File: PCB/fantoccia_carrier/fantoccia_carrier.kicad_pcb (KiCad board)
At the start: 2 copper layers, 108 x 131.5 mm, 13 parts, among them J1 BU2450SM-JJ-GTR, J2 1881545, J3 1881545, J4 1881545, J5 1881545, U1 NUCLEO144-H743ZI, U2 TXS0108EPWR, U3 TXS0108EPWR

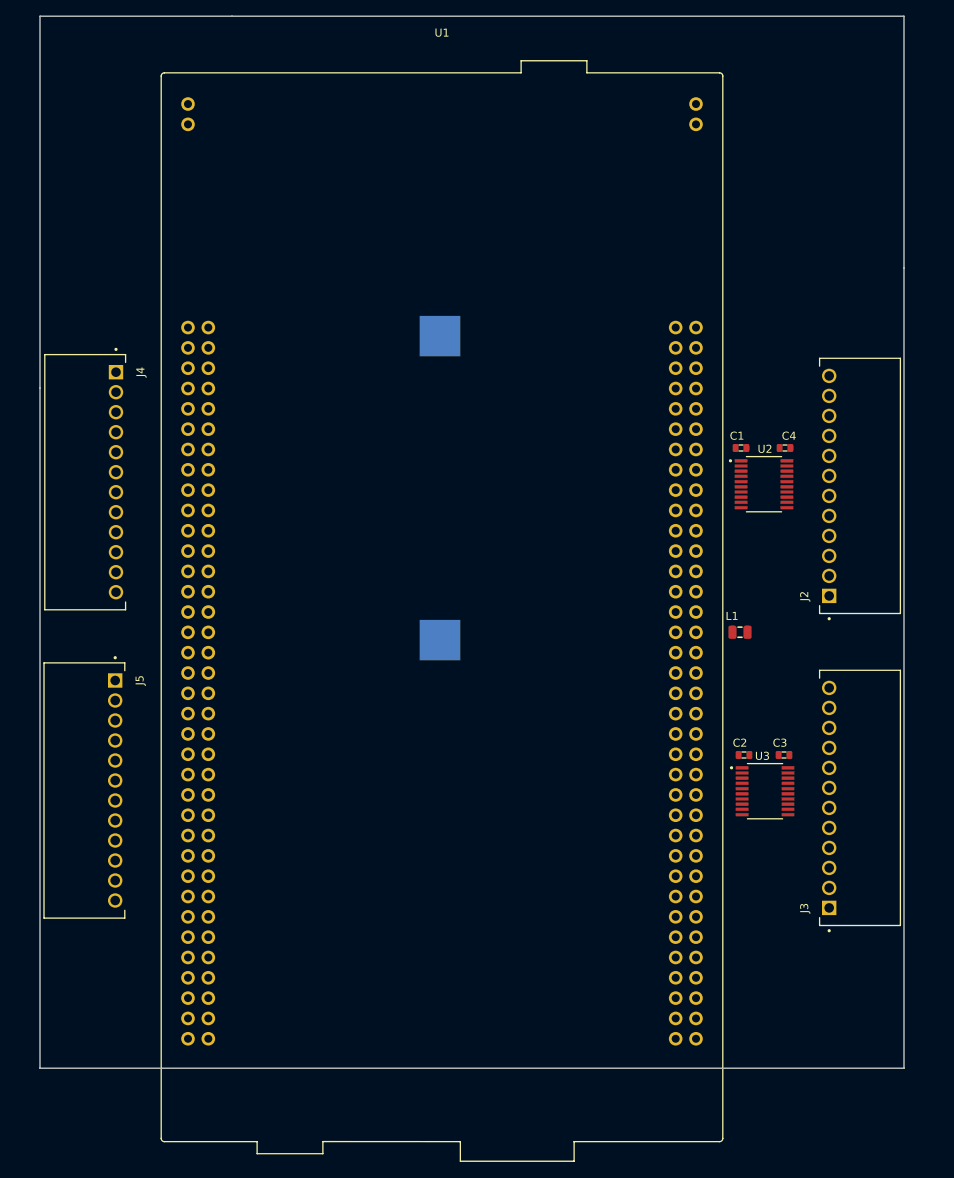
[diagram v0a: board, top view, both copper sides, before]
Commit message: PCB progress and feature updates
Added another bank of 5V channels. PCB layout figured out, board shape defined. 3D model added to STM32 evaluation kit. Now just need to determine pinout and add protection circuitry to pins.
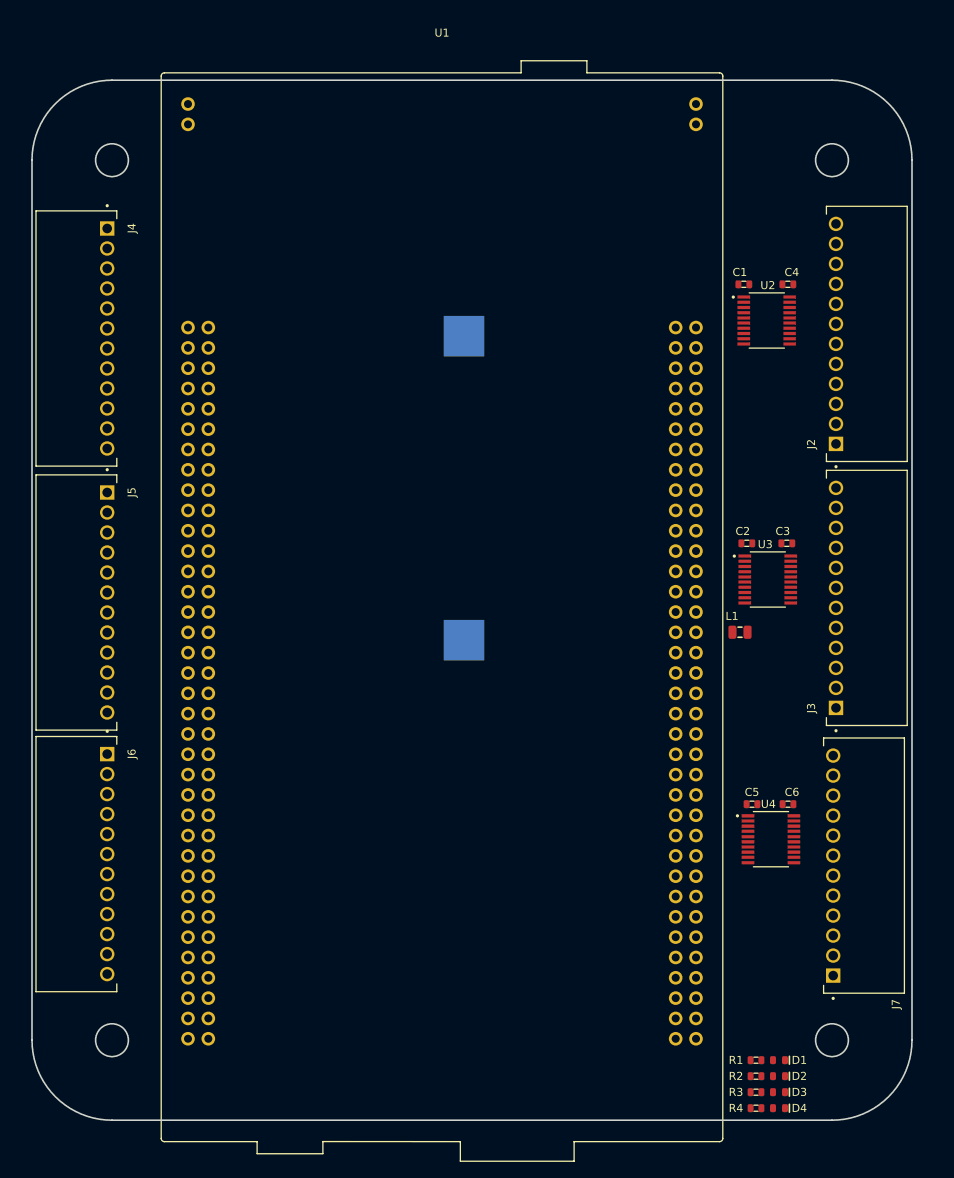
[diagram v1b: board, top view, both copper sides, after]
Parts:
- added C5: CGA3E2X7R1H104K080AA, AVR-KiCAD-Lib-Capacitors:C0603, F.Cu at (194.0, 117.0)
- added C6: CGA3E2X7R1H104K080AA, AVR-KiCAD-Lib-Capacitors:C0603, F.Cu at (198.5, 117.0)
- added D1: LTST-C194TBKT, AVR-KiCAD-Lib-Diodes:LED0603, F.Cu at (197.4, 149.0)
- added D2: LTST-C194TBKT, AVR-KiCAD-Lib-Diodes:LED0603, F.Cu at (197.4, 151.0)
- added D3: LTST-C194TBKT, AVR-KiCAD-Lib-Diodes:LED0603, F.Cu at (197.4, 153.0)
- added D4: LTST-C194TBKT, AVR-KiCAD-Lib-Diodes:LED0603, F.Cu at (197.4, 155.0)
- added J6: 1881545, AVR-KiCAD-Lib-Connectors:PHOENIX_1881545, F.Cu at (104.5, 108.5)
- added J7: 1881545, AVR-KiCAD-Lib-Connectors:PHOENIX_1881545, F.Cu at (213.1, 140.6)
- added R1: RC0603FR-072K2L, AVR-KiCAD-Lib-Resistors:R0603, F.Cu at (194.5, 149.0)
- added R2: RC0603FR-072K2L, AVR-KiCAD-Lib-Resistors:R0603, F.Cu at (194.5, 151.0)
- added R3: RC0603FR-072K2L, AVR-KiCAD-Lib-Resistors:R0603, F.Cu at (194.5, 153.0)
- added R4: RC0603FR-072K2L, AVR-KiCAD-Lib-Resistors:R0603, F.Cu at (194.5, 155.0)
- added U4: TXS0108EPWR, AVR-KiCAD-Lib-ICs:SOP65P640X120-20N, F.Cu at (196.4, 121.4)
- moved U3 26.5 mm to (196.0, 88.9)
- moved C2 26.5 mm to (193.3, 84.4)
- moved C3 26.5 mm to (198.3, 84.4)
- moved J3 25.0 mm to (213.4, 107.2)
- moved J5 23.5 mm to (104.5, 75.8)
- moved U2 20.5 mm to (195.8, 56.5)
- moved C1 20.5 mm to (193.0, 52.0)
- moved C4 20.5 mm to (198.5, 52.0)
- moved J2 19.0 mm to (213.4, 74.2)
- moved J4 18.0 mm to (104.5, 42.8)
- moved J1 3.00 mm to (158.0, 77.5)
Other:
- board size 108 x 131.5 mm -> 110 x 130 mm

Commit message: Design Rules
Created Design rules, added more IO connections, need to figure out pinning next.
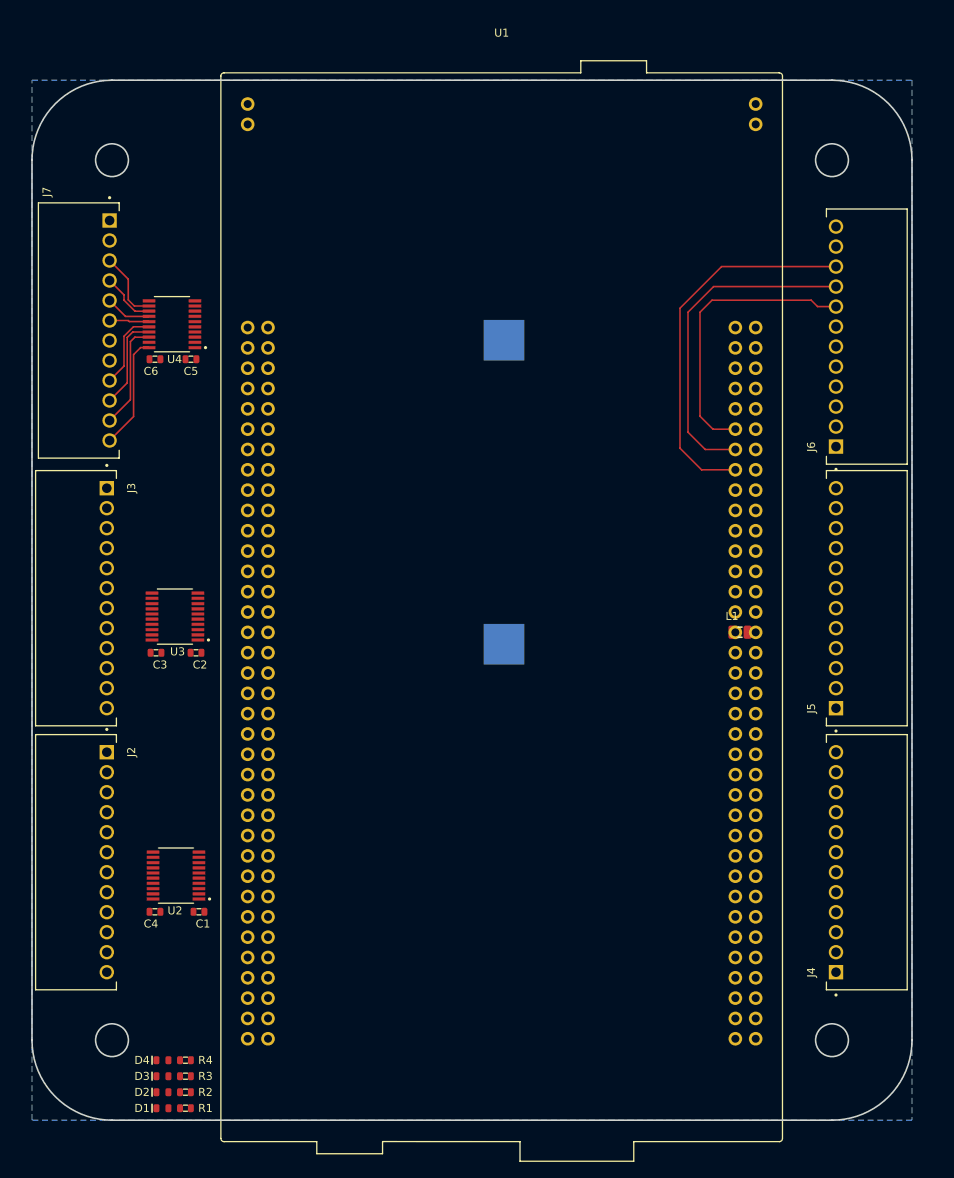
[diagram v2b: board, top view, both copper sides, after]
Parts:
- moved J7 146.6 mm to (104.8, 41.8), turned to -90 degrees
- moved J4 146.1 mm to (213.4, 140.2), turned to 90 degrees
- moved J2 114.2 mm to (104.5, 108.3), turned to -90 degrees
- moved J6 114.1 mm to (213.4, 74.5), turned to 90 degrees
- moved J3 113.5 mm to (104.5, 75.3), turned to -90 degrees
- moved J5 113.3 mm to (213.4, 107.2), turned to 90 degrees
- moved C4 111.4 mm to (119.4, 130.4), turned to 180 degrees
- moved C1 103.9 mm to (124.9, 130.4), turned to 0 degrees
- moved U2 101.3 mm to (122.0, 125.9), turned to 180 degrees
- moved U4 98.7 mm to (121.5, 57.0), turned to 180 degrees
- moved C6 96.7 mm to (119.4, 61.4), turned to 180 degrees
- moved C5 89.5 mm to (123.9, 61.4), turned to 0 degrees
- moved C3 80.0 mm to (119.5, 98.1), turned to 180 degrees
- moved D1 77.3 mm to (120.3, 155.0), turned to 180 degrees
- moved D4 77.3 mm to (120.3, 149.0), turned to 180 degrees
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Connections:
- J6 pad 1: unconnected-(J6-Pin_1-Pad1) -> /Nucleo/3.3V_GPIO16
- J6 pad 10: unconnected-(J6-Pin_10-Pad10) -> /Nucleo/3.3V_GPIO23
- J6 pad 2: unconnected-(J6-Pin_2-Pad2) -> /Nucleo/3.3V_GPIO17
- J6 pad 3: unconnected-(J6-Pin_3-Pad3) -> /Nucleo/3.3V_GPIO18
- J6 pad 4: unconnected-(J6-Pin_4-Pad4) -> /Nucleo/3.3V_GPIO19
- J6 pad 7: unconnected-(J6-Pin_7-Pad7) -> /Nucleo/3.3V_GPIO20
- J6 pad 8: unconnected-(J6-Pin_8-Pad8) -> /Nucleo/3.3V_GPIO21
- J6 pad 9: unconnected-(J6-Pin_9-Pad9) -> /Nucleo/3.3V_GPIO22
- U1 pad 83: unconnected-(U1-PA5-Pad83) -> /Nucleo/3.3V_GPIO21
- U1 pad 85: unconnected-(U1-PA6-Pad85) -> /Nucleo/3.3V_GPIO22
- U1 pad 87: unconnected-(U1-ETH_CRS_DV/PA7-Pad87) -> /Nucleo/3.3V_GPIO23
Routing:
- net /Nucleo/3.3V_GPIO23: track 0.00 -> 47.2 mm
- net /Nucleo/3.3V_GPIO22: track 0.00 -> 41.6 mm
- net /Nucleo/3.3V_GPIO21: track 0.00 -> 36.0 mm
- net /Translator 5V/5V_GPIO16: track 0.00 -> 14.3 mm
- net /Translator 5V/5V_GPIO17: track 0.00 -> 13.5 mm
- net /Translator 5V/5V_GPIO18: track 0.00 -> 11.8 mm
- net /Translator 5V/5V_GPIO19: track 0.00 -> 9.90 mm
- net /Translator 5V/5V_GPIO23: track 0.00 -> 8.81 mm
- net /Translator 5V/5V_GPIO22: track 0.00 -> 6.91 mm
- net /Translator 5V/5V_GPIO21: track 0.00 -> 5.75 mm
- net /Translator 5V/5V_GPIO20: track 0.00 -> 4.99 mm
- added copper zone on B.Cu, net GND

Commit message: PCB and Pinout
Progress made with PCB wiring eval board pins to pheonix connectors. Pinout almost completely chosen but subject to revision !
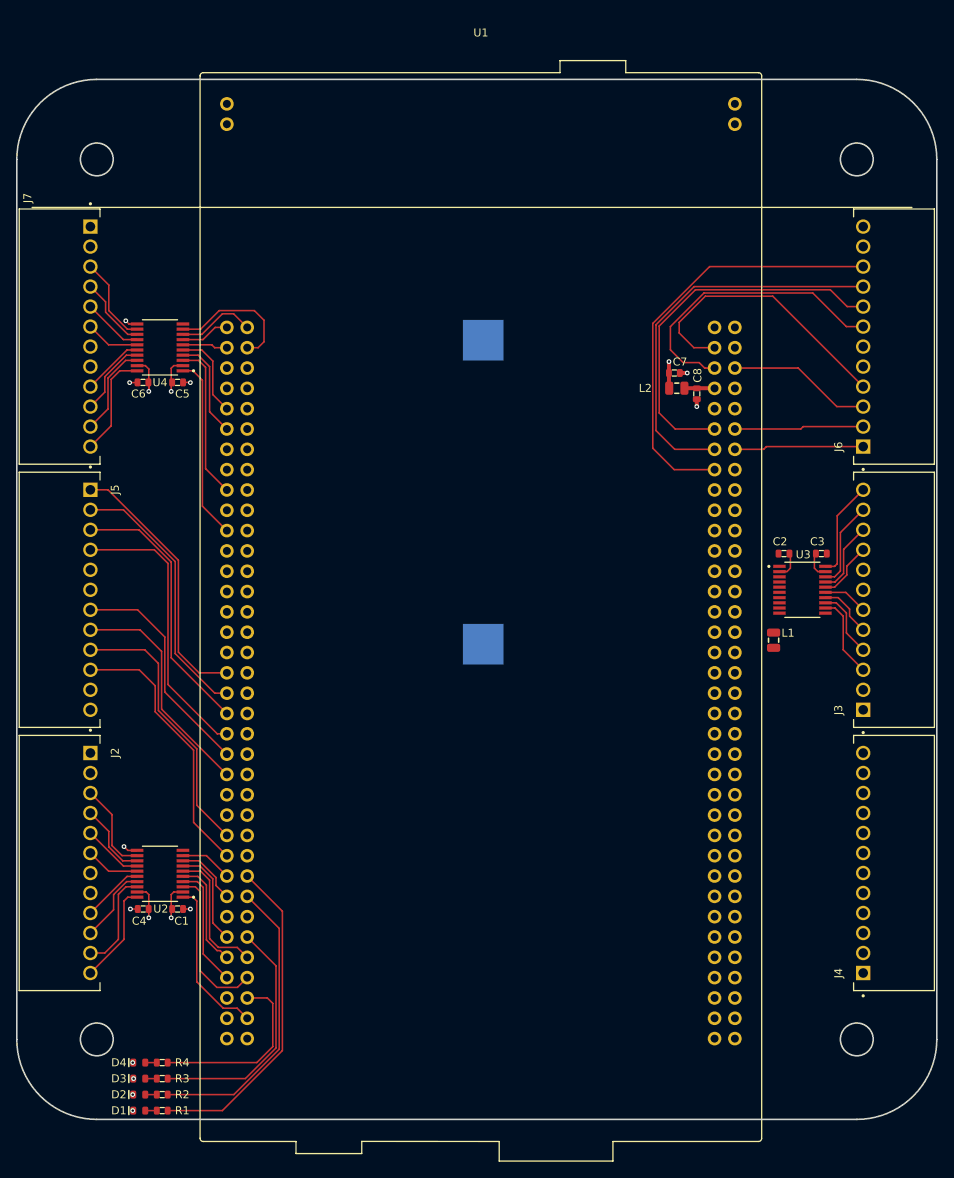
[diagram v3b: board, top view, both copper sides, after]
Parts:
- added C7: CGA3E2X7R1H104K080AA, AVR-KiCAD-Lib-Capacitors:C0603, F.Cu at (184.3, 63.1)
- added C8: CGA3E2X7R1H104K080AA, AVR-KiCAD-Lib-Capacitors:C0603, F.Cu at (187.1, 65.7)
- added L2: HZ0805E601R-10, AVR-KiCAD-Lib-Inductors:HZ0805E601R-10, F.Cu at (184.6, 65.0)
- moved J3 116.8 mm to (216.8, 107.4), turned to 90 degrees
- moved J5 115.4 mm to (102.4, 75.5), turned to -90 degrees
- moved C3 84.1 mm to (202.7, 85.7), turned to 0 degrees
- moved U3 78.5 mm to (200.3, 90.2), turned to 0 degrees
- moved C2 74.5 mm to (198.0, 85.7), turned to 180 degrees
- moved L1 4.32 mm to (196.7, 96.5), turned to -90 degrees
- moved J4 3.40 mm to (216.8, 140.3)
- moved J6 3.40 mm to (216.8, 74.5)
- moved C5 3.35 mm to (122.2, 64.3)
- moved C6 3.26 mm to (117.9, 64.3)
- moved U4 3.26 mm to (120.0, 59.9)
- moved D1 2.92 mm to (117.4, 155.3)
- moved D2 2.92 mm to (117.4, 153.3)
- moved D3 2.92 mm to (117.4, 151.3)
- moved D4 2.92 mm to (117.4, 149.3)
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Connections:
- R1 pad 1: unconnected-(R1-Pad1) -> /Nucleo/LED2
- R2 pad 1: unconnected-(R2-Pad1) -> /Nucleo/LED3
- R3 pad 1: unconnected-(R3-Pad1) -> /Nucleo/LED1
- R4 pad 1: unconnected-(R4-Pad1) -> /Nucleo/LED0
- U1 pad 1: unconnected-(U1-PC10-Pad1) -> /Nucleo/CV_GPIO21
- U1 pad 11: unconnected-(U1-PF7-Pad11) -> /Nucleo/CV_GPIO18
- U1 pad 12: unconnected-(U1-IOREF-Pad12) -> /Nucleo/RESERVED_3
- U1 pad 14: unconnected-(U1-~{RST}-Pad14) -> /Nucleo/RESERVED_7
- U1 pad 16: unconnected-(U1-+3V3-Pad16) -> /Nucleo/RESERVED_2
- U1 pad 17: unconnected-(U1-PA15-Pad17) -> /Nucleo/CV_GPIO17
- U1 pad 18: unconnected-(U1-+5V-Pad18) -> /Nucleo/RESERVED_1
- U1 pad 2: unconnected-(U1-PC11-Pad2) -> /Nucleo/CV_GPIO22
- U1 pad 21: unconnected-(U1-LD2/PB7-Pad21) -> /Nucleo/CV_GPIO16
- U1 pad 24: unconnected-(U1-VIN-Pad24) -> /Nucleo/RESERVED_0
- U1 pad 3: unconnected-(U1-PC12-Pad3) -> /Nucleo/CV_GPIO20
- U1 pad 35: unconnected-(U1-PC2-Pad35) -> /Nucleo/3.3V_GPIO0
- U1 pad 37: unconnected-(U1-PC3-Pad37) -> /Nucleo/3.3V_GPIO1
- U1 pad 39: unconnected-(U1-PD4-Pad39) -> /Nucleo/3.3V_GPIO2
- U1 pad 4: unconnected-(U1-PD2-Pad4) -> /Nucleo/CV_GPIO23
- U1 pad 41: unconnected-(U1-PD5-Pad41) -> /Nucleo/3.3V_GPIO3
- U1 pad 43: unconnected-(U1-PD6-Pad43) -> /Nucleo/3.3V_GPIO4
- U1 pad 45: unconnected-(U1-PD7-Pad45) -> /Nucleo/3.3V_GPIO5
- U1 pad 5: unconnected-(U1-VDD-Pad5) -> /Nucleo/RESERVED_5
- U1 pad 51: unconnected-(U1-PF1-Pad51) -> /Nucleo/3.3V_GPIO6
- U1 pad 53: unconnected-(U1-PF0-Pad53) -> /Nucleo/3.3V_GPIO7
- U1 pad 55: unconnected-(U1-PD1-Pad55) -> /Nucleo/CV_GPIO7
- U1 pad 56: unconnected-(U1-PF9-Pad56) -> /Nucleo/LED2
- U1 pad 57: unconnected-(U1-PD0-Pad57) -> /Nucleo/CV_GPIO6
- U1 pad 58: unconnected-(U1-PG1-Pad58) -> /Nucleo/LED3
- U1 pad 6: unconnected-(U1-E5V-Pad6) -> /Nucleo/RESERVED_4
- U1 pad 61: unconnected-(U1-PE1-Pad61) -> /Nucleo/CV_GPIO5
- U1 pad 62: unconnected-(U1-PE6-Pad62) -> /Nucleo/LED1
- U1 pad 63: unconnected-(U1-PG9-Pad63) -> /Nucleo/CV_GPIO3
- U1 pad 64: unconnected-(U1-PG15-Pad64) -> /Nucleo/CV_GPIO4
- U1 pad 65: unconnected-(U1-PG12-Pad65) -> /Nucleo/CV_GPIO2
- U1 pad 66: unconnected-(U1-PG10-Pad66) -> /Nucleo/CV_GPIO1
- U1 pad 68: unconnected-(U1-PG13/ETH_TXD0-Pad68) -> /Nucleo/LED0
- U1 pad 7: unconnected-(U1-~{BOOT0}-Pad7) -> /Nucleo/RESERVED_6
- U1 pad 70: unconnected-(U1-PG11/ETH_TX_EN-Pad70) -> /Nucleo/CV_GPIO0
- U1 pad 75: unconnected-(U1-PB8-Pad75) -> /Nucleo/3.3V_GPIO19
- U1 pad 77: unconnected-(U1-PB9-Pad77) -> /Nucleo/3.3V_GPIO20
- U1 pad 78: unconnected-(U1-ETH_RXD1/PC5-Pad78) -> /Nucleo/3.3V_GPIO18
- U1 pad 79: unconnected-(U1-AVDD-Pad79) -> Net-(U1-AVDD)
- U1 pad 80: unconnected-(U1-U5V-Pad80) -> /Nucleo/RESERVED_8
- U1 pad 84: unconnected-(U1-USB_DP/PA12-Pad84) -> /Nucleo/3.3V_GPIO17
- U1 pad 86: unconnected-(U1-USB_DM/PA11-Pad86) -> /Nucleo/3.3V_GPIO16
- U1 pad 9: unconnected-(U1-PF6-Pad9) -> /Nucleo/CV_GPIO19
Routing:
- net /Nucleo/LED2: track 0.00 -> 41.1 mm
- net /Nucleo/LED3: track 0.00 -> 37.1 mm
- net /Nucleo/3.3V_GPIO20: track 0.00 -> 36.9 mm
- net /Nucleo/3.3V_GPIO19: track 0.00 -> 35.5 mm
- net /Nucleo/3.3V_GPIO3: track 0.00 -> 35.5 mm
- net /Nucleo/3.3V_GPIO6: track 0.00 -> 34.2 mm
- net /Nucleo/3.3V_GPIO7: track 0.00 -> 33.9 mm
- net /Nucleo/3.3V_GPIO2: track 0.00 -> 33.6 mm
- net /Nucleo/3.3V_GPIO1: track 0.00 -> 33.3 mm
- net /Nucleo/3.3V_GPIO0: track 0.00 -> 33.3 mm
- net /Nucleo/LED1: track 0.00 -> 30.5 mm
- net /Nucleo/3.3V_GPIO5: track 0.00 -> 28.8 mm
- net /Nucleo/3.3V_GPIO4: track 0.00 -> 28.6 mm
- net /Nucleo/CV_GPIO16: track 0.00 -> 23.0 mm
- net /Nucleo/LED0: track 0.00 -> 22.9 mm
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- added copper zone on In2.Cu, net +3.3V
- added copper zone on In1.Cu, net GND
- removed copper zone on B.Cu, net GND
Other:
- board size 110 x 130 mm -> 115 x 130 mm
- copper layers 2 -> 4
